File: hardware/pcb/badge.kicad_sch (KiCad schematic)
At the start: 57 parts, among them J1 EPD FPC 24P 0.5mm, J2 BATT JST-SH 1.0mm, J3 USB-C 16P 沉板 (TYPE-C-31-M-14), Q1 AO3400A, Q2 AO3401A, SW1 RESET, SW2 BOOT/USER, U1 ESP32-C3-MINI-1-N4, U2 ST25DV64KC-IER6S3, U3 TP4054 / MCP73831T-2ACI/OT, U4 XC6220B331MR-G

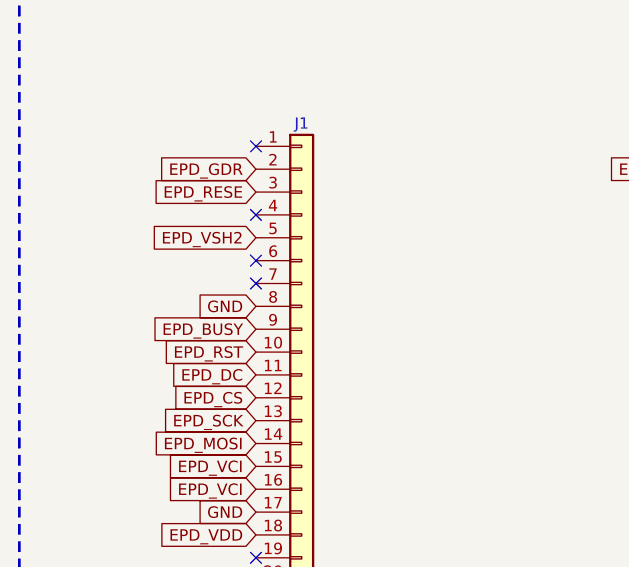
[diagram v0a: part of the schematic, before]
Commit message: Stitch GND pour islands to DRC-clean PCB and write handoff for next session
Current board is 564 tracks / 128 vias with zero DRC errors. route_pcb.py
gains island stitching, J1 pin 7 to GND, ESP GND net-tie, and via nudge.
Handoff and review checklist capture remaining work: make stitching
reproducible, NFC soldermask, fab review, firmware.

Co-authored-by: kongm3270 <kongm3270@outlook.com>
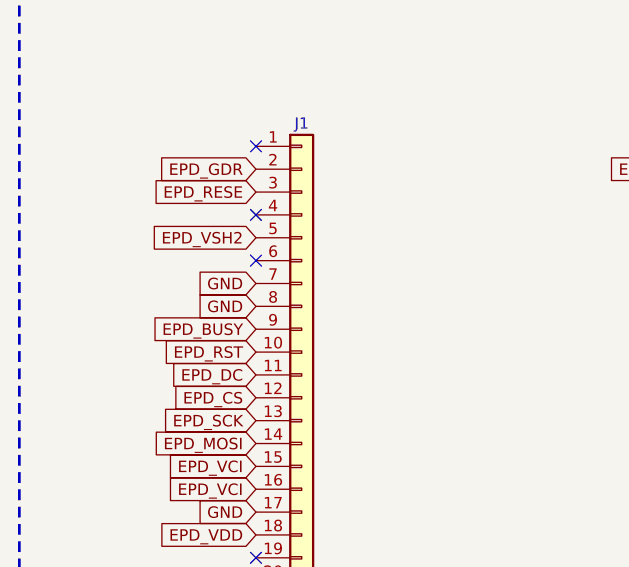
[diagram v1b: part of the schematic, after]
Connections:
- net GND: now also J1.7 (Pin_7)
- no-connect marks 22 -> 21
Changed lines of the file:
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@@
   )
   (no_connect (at 34.29 360.68))
-  (no_connect (at 34.29 363.22))
+  (global_label "GND" (shape input) (at 34.29 363.22 180) (fields_autoplaced yes)
+    (effects (font (size 1.27 1.27)) (justify right))
+    (property "Intersheetrefs" "${INTERSHEET_REFS}" (at 34.29 363.22 0) (effects (font (size 1.27 1.27)) (hide yes)))
+  )
   (global_label "GND" (shape input) (at 34.29 365.76 180) (fields_autoplaced yes)
     (effects (font (size 1.27 1.27)) (justify right))
